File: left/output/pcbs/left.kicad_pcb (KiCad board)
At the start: 2 copper layers, 120 x 98 mm, 55 parts

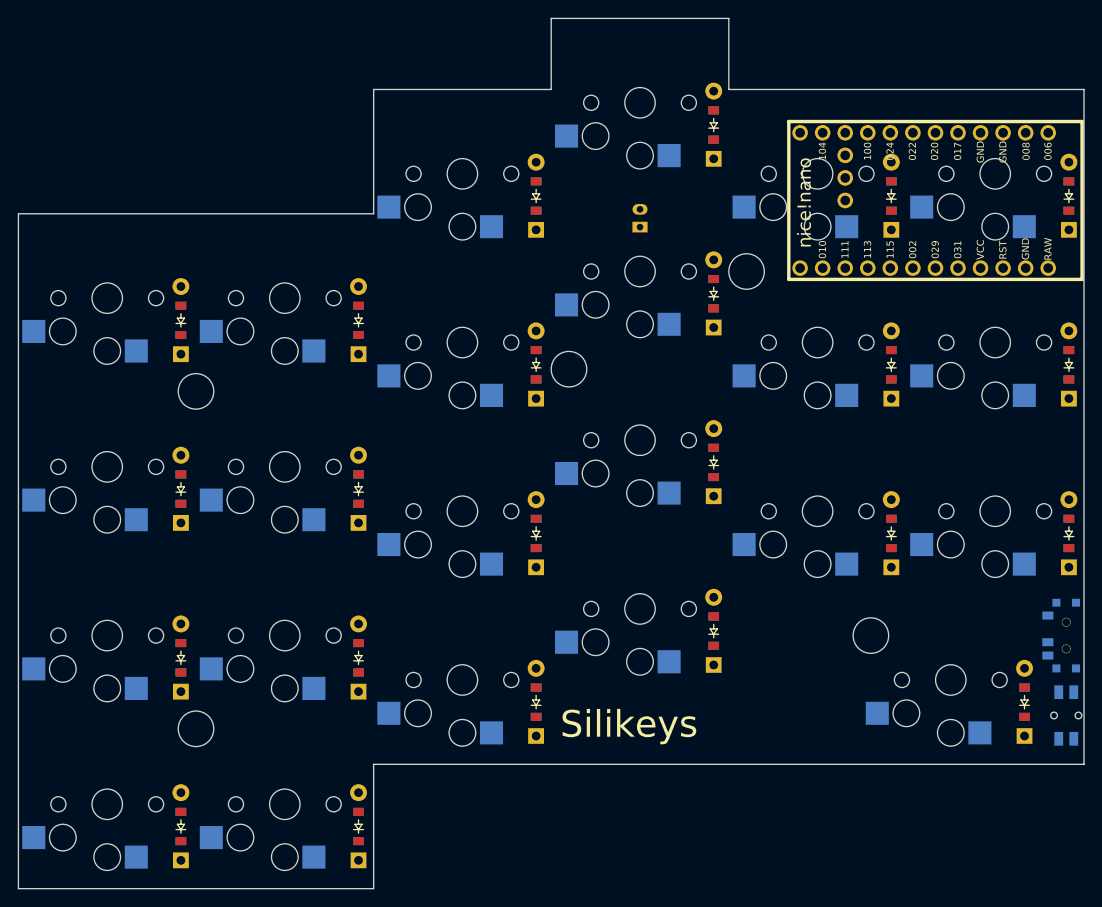
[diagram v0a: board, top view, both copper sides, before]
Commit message: started the new pcb for the left side
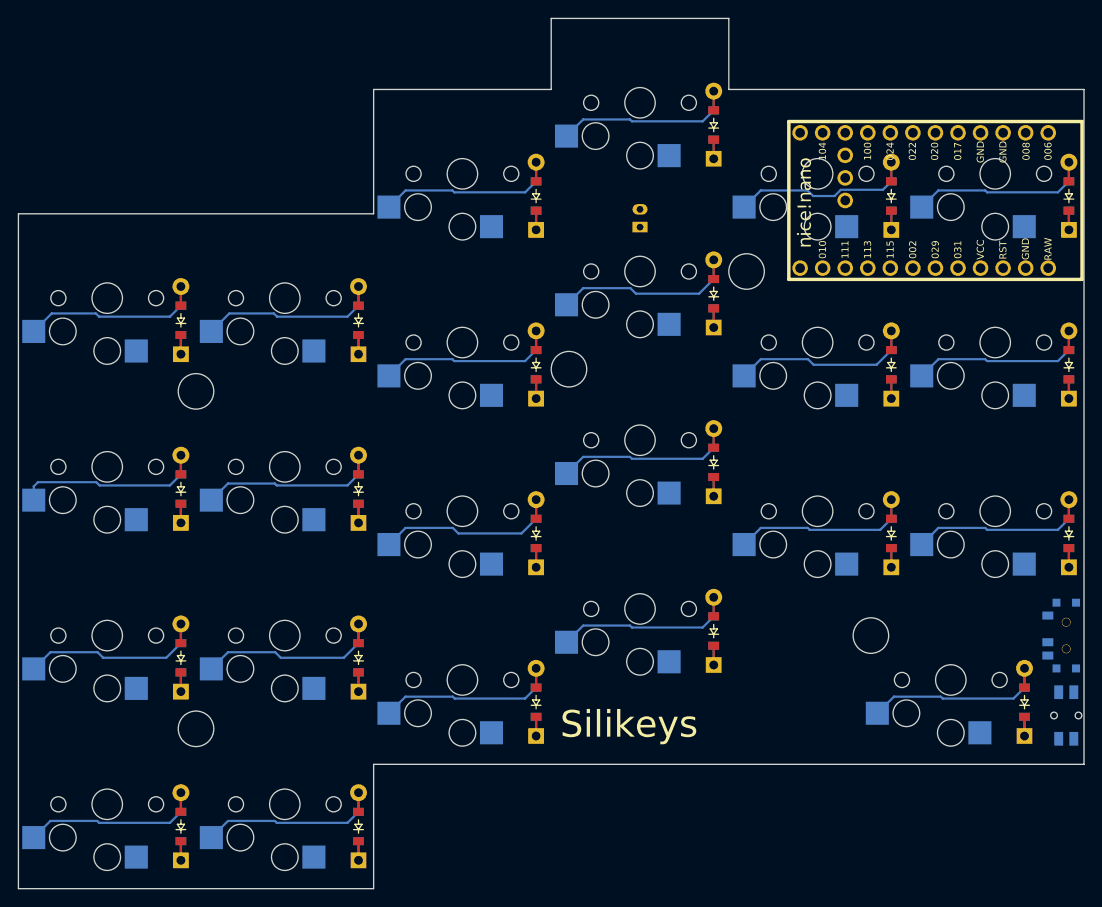
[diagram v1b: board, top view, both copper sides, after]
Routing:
- net P115: track 0.00 -> 25.9 mm
- net P113: track 0.00 -> 25.9 mm
- net P002: track 0.00 -> 25.9 mm
- net shift_home: track 0.00 -> 23.3 mm
- net a_down: track 0.00 -> 22.6 mm
- net s_down: track 0.00 -> 22.6 mm
- net f_up: track 0.00 -> 22.6 mm
- net f_home: track 0.00 -> 22.6 mm
- net d_home: track 0.00 -> 22.6 mm
- net shift_down: track 0.00 -> 22.6 mm
- net a_up: track 0.00 -> 22.4 mm
- net shift_up: track 0.00 -> 22.4 mm
- net s_up: track 0.00 -> 22.3 mm
- net s_home: track 0.00 -> 22.3 mm
- net g_up: track 0.00 -> 22.3 mm
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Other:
- net class Default removed
